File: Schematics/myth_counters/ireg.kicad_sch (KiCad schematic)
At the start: 8 parts, among them U10 74HC157, U11 74HC157, U12 74HC193, U13 74HC193, U14 4078, U15 74AHC574, U5 74HC02, U7 74LS32

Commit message: Change d to g
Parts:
- U5, U7: footprint (none) -> Package_DIP:DIP-14_W7.62mm_LongPads
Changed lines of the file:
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@@
 			)
 		)
-		(property "Footprint" ""
+		(property "Footprint" "Package_DIP:DIP-14_W7.62mm_LongPads"
 			(at 208.28 144.78 0)
 			(effects
@@
 			)
 		)
-		(property "Footprint" ""
+		(property "Footprint" "Package_DIP:DIP-14_W7.62mm_LongPads"
 			(at 53.34 170.18 0)
 			(effects
@@
 			)
 		)
-		(property "Footprint" ""
+		(property "Footprint" "Package_DIP:DIP-14_W7.62mm_LongPads"
 			(at 68.58 154.94 0)
 			(effects

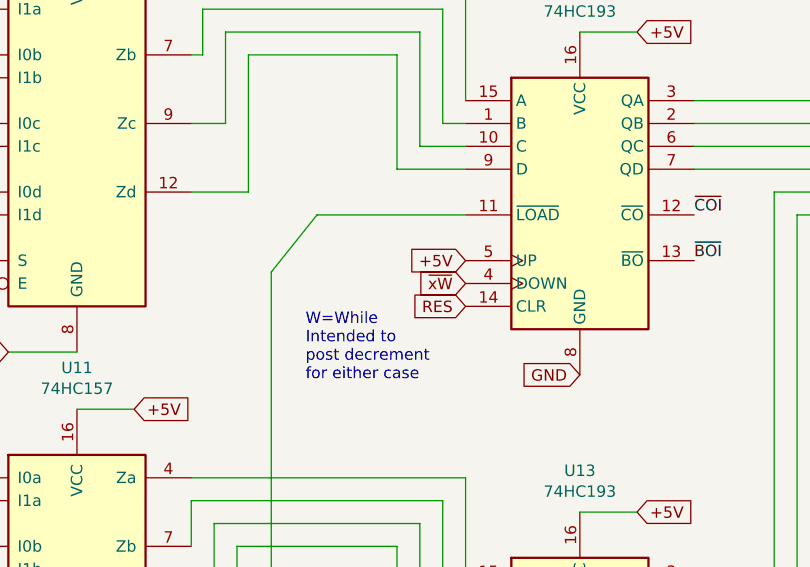
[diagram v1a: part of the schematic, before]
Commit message: Change signal names
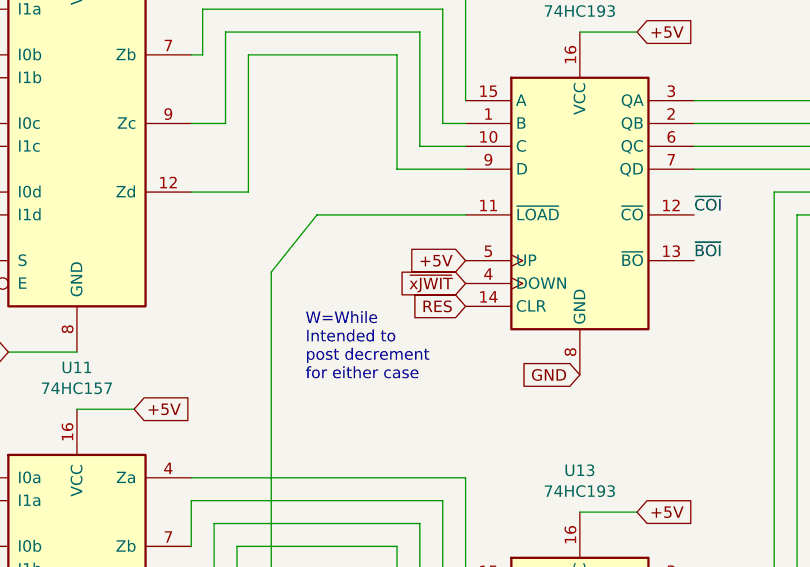
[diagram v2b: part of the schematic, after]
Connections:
- net ~{xW} renamed ~{xJWIT}
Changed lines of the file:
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@@
 		)
 	)
-	(global_label "~{xW}"
+	(global_label "~{xJWIT}"
 		(shape input)
 		(at 127 86.36 180)
